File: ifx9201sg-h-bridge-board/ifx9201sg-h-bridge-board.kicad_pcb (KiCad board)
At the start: 2 copper layers, 28 parts, among them J1 Conn_01x06, J2 1935161, J3 S6B-PH-K-S(LF)(SN), Q1 AOD407, U1 74LVC2G17, U2 IFX9201SG

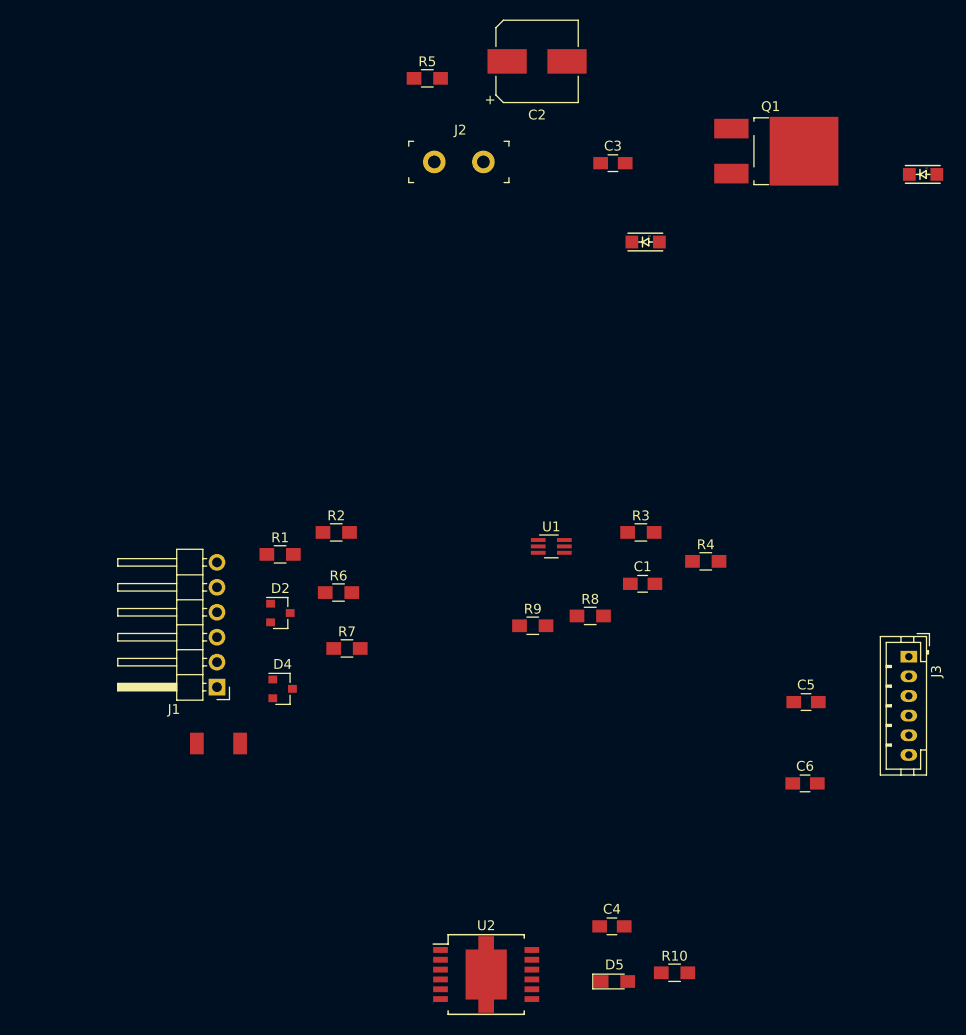
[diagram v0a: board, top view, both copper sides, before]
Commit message: During dev: PCB done except texts.
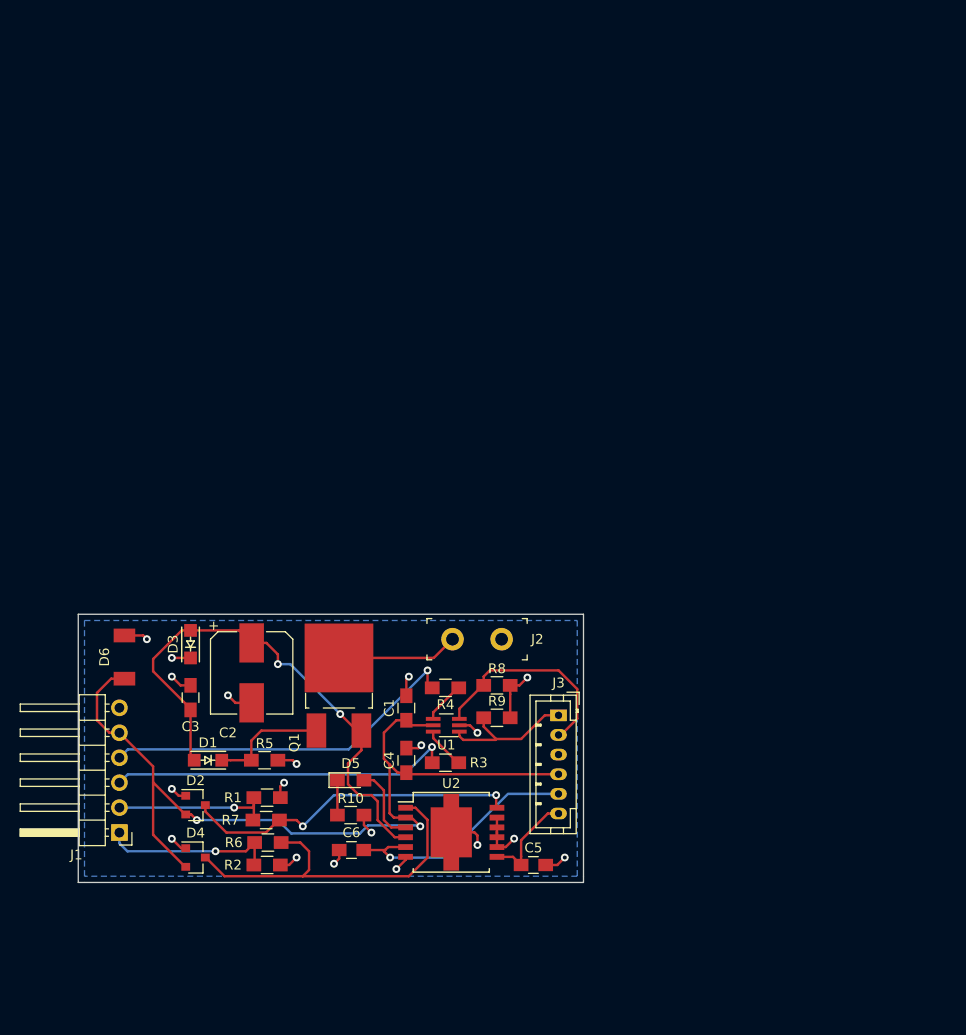
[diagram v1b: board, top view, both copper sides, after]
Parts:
- moved D1 94.1 mm to (137.0, 105.7), turned to 180 degrees
- moved R5 71.4 mm to (142.8, 105.7)
- moved Q1 70.3 mm to (150.4, 98.1), turned to 90 degrees
- moved C3 69.4 mm to (135.3, 99.3), turned to 90 degrees
- moved C2 68.7 mm to (141.5, 96.8), turned to 270 degrees
- moved D3 61.8 mm to (135.3, 93.8), turned to 90 degrees
- moved J2 48.6 mm to (161.9, 93.3)
- moved C6 46.7 mm to (151.6, 114.8), turned to 180 degrees
- moved R10 36.7 mm to (151.6, 111.3)
- moved J3 36.2 mm to (172.7, 101.1)
- moved R2 34.6 mm to (143.0, 116.3)
- moved D5 33.8 mm to (151.6, 107.7)
- moved C5 32.3 mm to (170.2, 116.3)
- moved R3 30.7 mm to (161.2, 105.9), turned to 180 degrees
- moved R4 29.5 mm to (161.2, 98.3), turned to 180 degrees
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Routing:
- net VPP: track 0.00 -> 90.7 mm, vias 0 -> 2
- net Net-(C2-Pad1): track 0.00 -> 54.5 mm, vias 0 -> 2
- net GND: track 0.00 -> 46.9 mm, vias 0 -> 19
- net Net-(J1-Pad4): track 0.00 -> 37.0 mm, vias 0 -> 1
- net Net-(D4-Pad3): track 0.00 -> 36.8 mm
- net Net-(J1-Pad3): track 0.00 -> 34.9 mm, vias 0 -> 1
- net Net-(D2-Pad3): track 0.00 -> 34.6 mm, vias 0 -> 2
- net Net-(C6-Pad1): track 0.00 -> 25.3 mm, vias 0 -> 1
- net SB_IN: track 0.00 -> 21.6 mm
- net Net-(J1-Pad1): track 0.00 -> 17.9 mm, vias 0 -> 1
- net Net-(J1-Pad2): track 0.00 -> 17.0 mm, vias 0 -> 1
- net SA_IN: track 0.00 -> 14.4 mm
- net Net-(J2-Pad1): track 0.00 -> 12.3 mm
- net Net-(D1-Pad2): track 0.00 -> 12.1 mm
- net Net-(C5-Pad1): track 0.00 -> 10.3 mm
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- added copper zone on B.Cu, net GND
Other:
- board outline added: 51.4 x 27.3 mm

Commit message: PCB completed
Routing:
- net GND: track 46.9 -> 69.2 mm, vias 19 -> 30
- net VPP: track 90.7 -> 105.4 mm
- net Net-(C6-Pad1): track 25.3 -> 35.7 mm
- net Net-(D4-Pad3): track 36.8 -> 35.8 mm
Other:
- board text added: "+40V"
- board text added: "DIR"
- board text added: "EN"
- board text added: "GND"
- board text added: "IFX9201SG H-Bridge Board Rev -- Génie physique, Cégep La Pocatière"
- board text added: "SA"
- board text added: "SB"
- board text added: "VPP"
- board text added: "https://github.com/jscastonguay/IFX9201SG-H-Bridge-board"
- board text added: "max"

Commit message: Completed, Gerber produced.
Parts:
- R10: value 1.6k -> 150
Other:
- board text added: "K"
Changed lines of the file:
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@@
   (general
     (thickness 1.6)
-    (drawings 17)
+    (drawings 18)
     (tracks 273)
     (zones 0)
@@
     (pad_to_mask_clearance 0.051)
     (solder_mask_min_width 0.25)
+    (pad_to_paste_clearance_ratio -0.1)
     (aux_axis_origin 0 0)
     (visible_elements 7FFFFFFF)
     (pcbplotparams
-      (layerselection 0x010fc_ffffffff)
+      (layerselection 0x010f8_ffffffff)
       (usegerberextensions false)
       (usegerberattributes false)
@@
       (outputformat 1)
       (mirror false)
-      (drillshape 1)
+      (drillshape 0)
       (scaleselection 1)
-      (outputdirectory ""))
+      (outputdirectory "Gerber/"))
   )
   (net 0 "")
@@
       (effects (font (size 1 1) (thickness 0.15)))
     )
-    (fp_text value 1.6k (at 0 1.75) (layer F.Fab)
+    (fp_text value 150 (at 0 1.75) (layer F.Fab)
       (effects (font (size 1 1) (thickness 0.15)))
     )
@@
       (net 1 GND))
   )
+  (gr_text K (at 130.81 97.79) (layer F.SilkS)
+    (effects (font (size 1.5 1.5) (thickness 0.3)))
+  )
   (gr_text "IFX9201SG H-Bridge Board\nRev --\nGénie physique, Cégep La Pocatière" (at 160.655 102.87) (layer B.SilkS)
